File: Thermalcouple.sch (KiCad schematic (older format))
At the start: 14 parts

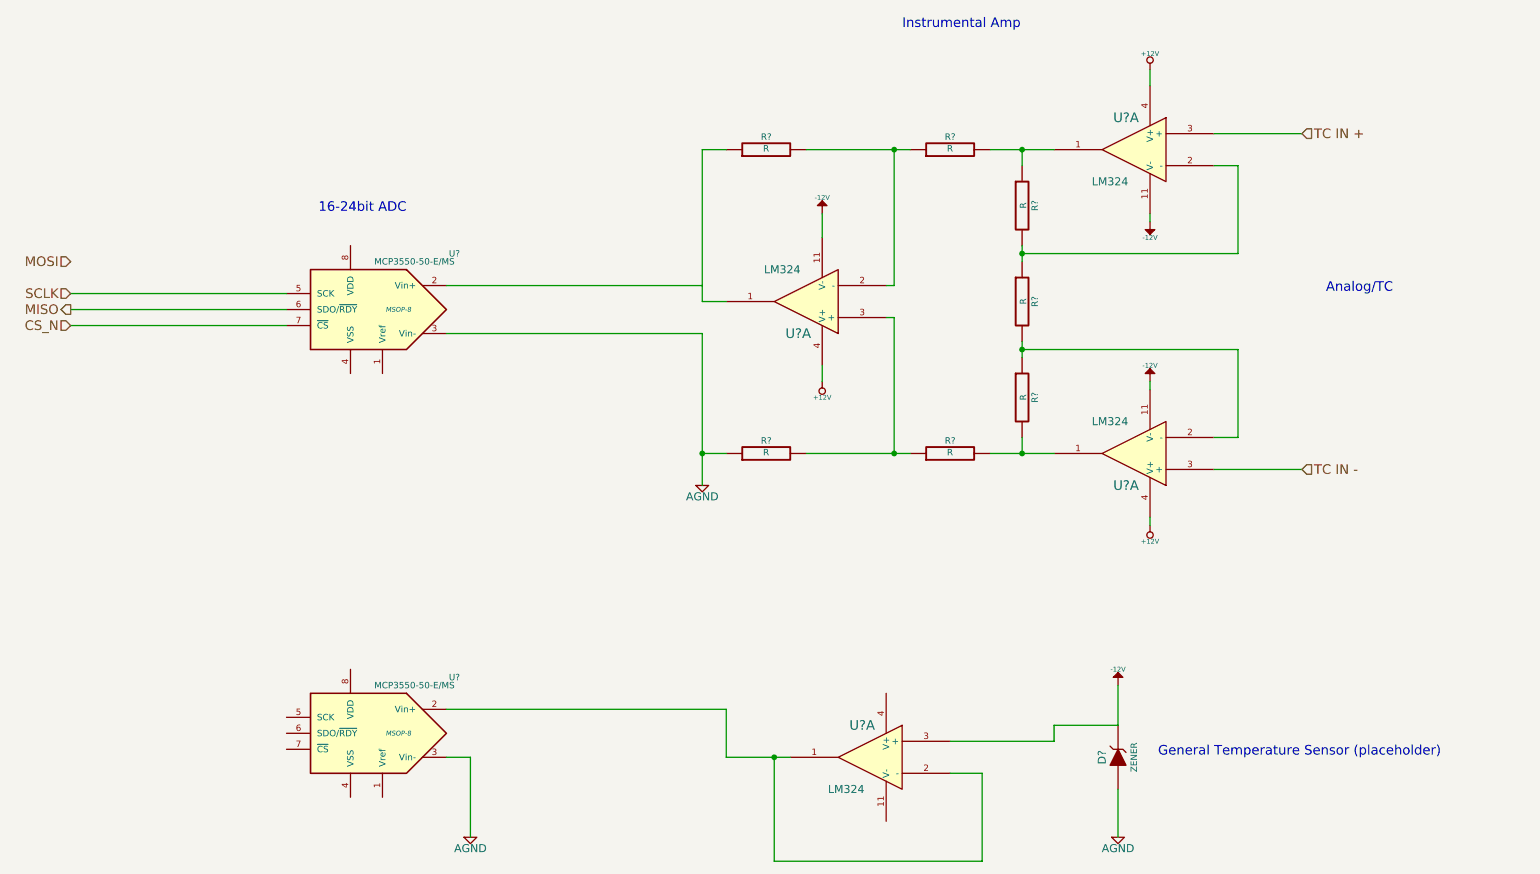
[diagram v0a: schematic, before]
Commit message: associating and placing relay module
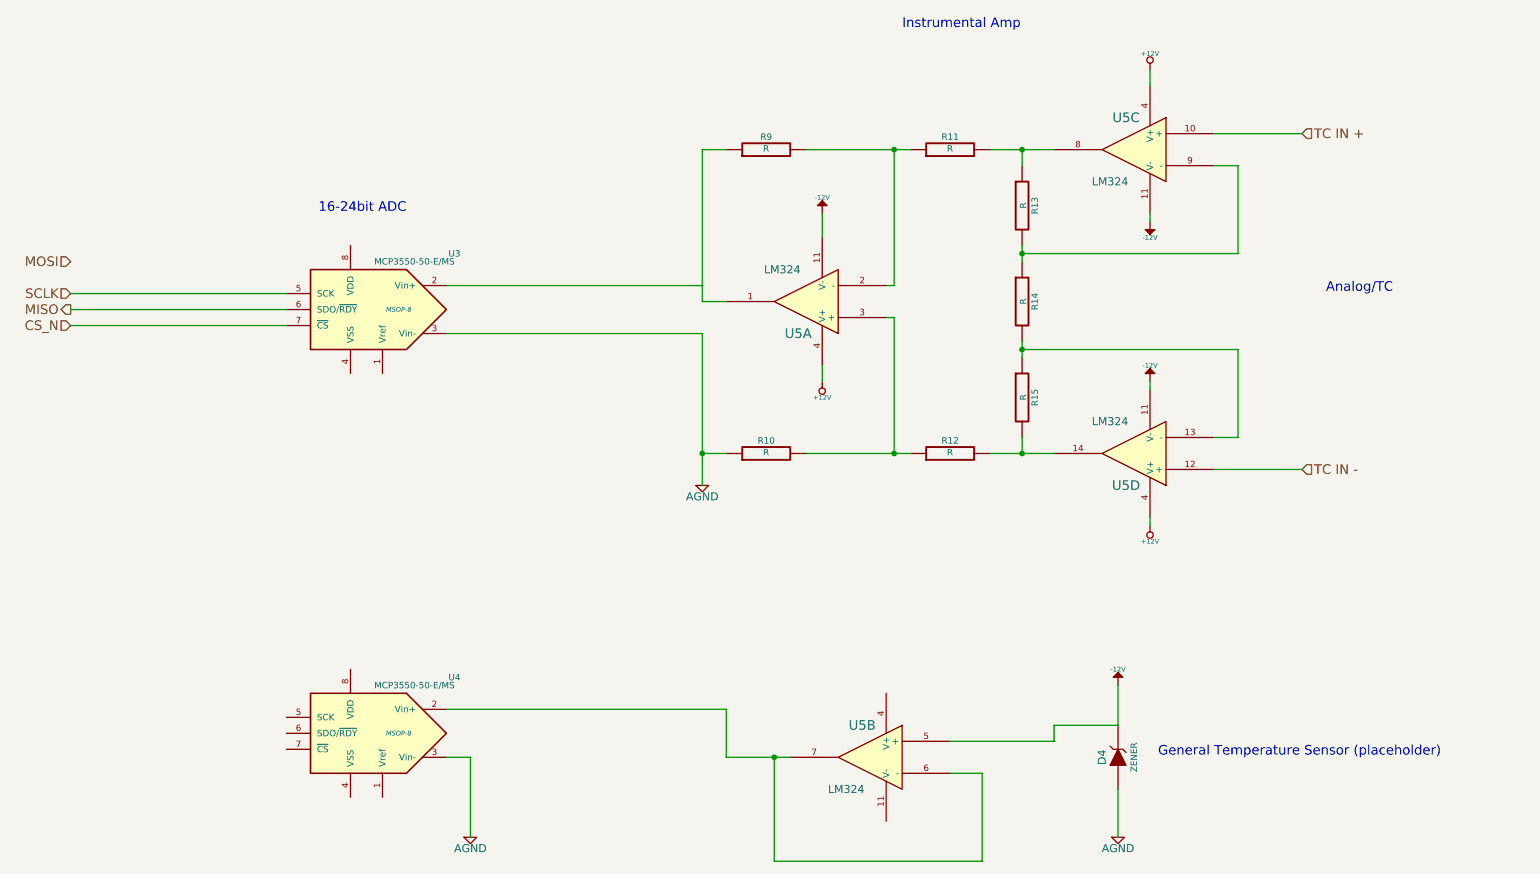
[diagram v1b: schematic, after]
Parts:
- gave numbers to parts that had none: 11
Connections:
- net -12V: now also U5.5 (+); no longer U5.3 (+)
- net TC IN +: now also U5.10 (+); no longer U5.3 (+)
- net TC IN -: now also U5.12 (+); no longer U5.3 (+)
- net at R11.2, R13.1: now also U5.8; no longer U5.1
- net at R13.2, R14.1: now also U5.9 (-); no longer U5.2 (-)
- net at R12.2, R15.2: now also U5.14; no longer U5.1
- net at R14.2, R15.1: now also U5.13 (-); no longer U5.2 (-)
- new net: U4.2 (Vin+), U5.6 (-), U5.7
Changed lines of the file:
@@
 Sheet 8 9
 Title ""
-Date "10 feb 2014"
+Date "22 feb 2014"
 Rev ""
 Comp ""
@@
 CS_N
 $Comp
-L LM324 U?
-U 1 1 52F0F265
+L LM324 U5
+U 3 1 52F0F265
 P 8500 2050
-F 0 "U?" H 8550 2250 60  0000 C CNN
+F 0 "U5" H 8550 2250 60  0000 C CNN
 F 1 "LM324" H 8650 1850 50  0000 C CNN
 F 2 "" H 8500 2050 60  0000 C CNN
 F 3 "" H 8500 2050 60  0000 C CNN
-	1    8500 2050
+	3    8500 2050
 	-1   0    0    -1
 $EndComp
 $Comp
-L LM324 U?
-U 1 1 52F0F27C
+L LM324 U5
+U 4 1 52F0F27C
 P 8500 3950
-F 0 "U?" H 8550 4150 60  0000 C CNN
+F 0 "U5" H 8550 4150 60  0000 C CNN
 F 1 "LM324" H 8650 3750 50  0000 C CNN
 F 2 "" H 8500 3950 60  0000 C CNN
 F 3 "" H 8500 3950 60  0000 C CNN
-	1    8500 3950
-	-1   0    0    1
-$EndComp
-$Comp
-L LM324 U?
+	4    8500 3950
+	-1   0    0    1
+$EndComp
+$Comp
+L LM324 U5
 U 1 1 52F0F282
 P 6450 3000
-F 0 "U?" H 6500 3200 60  0000 C CNN
+F 0 "U5" H 6500 3200 60  0000 C CNN
 F 1 "LM324" H 6600 2800 50  0000 C CNN
 F 2 "" H 6450 3000 60  0000 C CNN
@@
 $EndComp
 $Comp
-L LM324 U?
-U 1 1 52F0F288
+L LM324 U5
+U 2 1 52F0F288
 P 6850 5850
-F 0 "U?" H 6900 6050 60  0000 C CNN
+F 0 "U5" H 6900 6050 60  0000 C CNN
 F 1 "LM324" H 7000 5650 50  0000 C CNN
 F 2 "" H 6850 5850 60  0000 C CNN
 F 3 "" H 6850 5850 60  0000 C CNN
-	1    6850 5850
+	2    6850 5850
 	-1   0    0    -1
 $EndComp
 $Comp
-L R R?
+L R R13
 U 1 1 52F0F311
 P 7800 2400
-F 0 "R?" V 7880 2400 40  0000 C CNN
+F 0 "R13" V 7880 2400 40  0000 C CNN
 F 1 "R" V 7807 2401 40  0000 C CNN
 F 2 "~" V 7730 2400 30  0000 C CNN
@@
 $EndComp
 $Comp
-L R R?
+L R R14
 U 1 1 52F0F317
 P 7800 3000
-F 0 "R?" V 7880 3000 40  0000 C CNN
+F 0 "R14" V 7880 3000 40  0000 C CNN
 F 1 "R" V 7807 3001 40  0000 C CNN
 F 2 "~" V 7730 3000 30  0000 C CNN
@@
 $EndComp
 $Comp
-L R R?
+L R R15
 U 1 1 52F0F31D
 P 7800 3600
-F 0 "R?" V 7880 3600 40  0000 C CNN
+F 0 "R15" V 7880 3600 40  0000 C CNN
 F 1 "R" V 7807 3601 40  0000 C CNN
 F 2 "~" V 7730 3600 30  0000 C CNN
@@
 	7800 3950 7800 3850
 $Comp
-L R R?
+L R R11
 U 1 1 52F0F33D
 P 7350 2050
-F 0 "R?" V 7430 2050 40  0000 C CNN
+F 0 "R11" V 7430 2050 40  0000 C CNN
 F 1 "R" V 7357 2051 40  0000 C CNN
 F 2 "~" V 7280 2050 30  0000 C CNN
@@
 $EndComp
 $Comp
-L R R?
+L R R9
 U 1 1 52F0F349
 P 6200 2050
-F 0 "R?" V 6280 2050 40  0000 C CNN
+F 0 "R9" V 6280 2050 40  0000 C CNN
 F 1 "R" V 6207 2051 40  0000 C CNN
 F 2 "~" V 6130 2050 30  0000 C CNN
@@
 $EndComp
 $Comp
-L R R?
+L R R12
 U 1 1 52F0F360
 P 7350 3950
-F 0 "R?" V 7430 3950 40  0000 C CNN
+F 0 "R12" V 7430 3950 40  0000 C CNN
 F 1 "R" V 7357 3951 40  0000 C CNN
 F 2 "~" V 7280 3950 30  0000 C CNN
@@
 $EndComp
 $Comp
-L R R?
+L R R10
 U 1 1 52F0F366
 P 6200 3950
-F 0 "R?" V 6280 3950 40  0000 C CNN
+F 0 "R10" V 6280 3950 40  0000 C CNN
 F 1 "R" V 6207 3951 40  0000 C CNN
 F 2 "~" V 6130 3950 30  0000 C CNN
@@
 	9550 1950 9000 1950
 $Comp
-L -12V #PWR?
+L -12V #PWR023
 U 1 1 52F0F501
 P 6550 2450
-F 0 "#PWR?" H 6550 2580 20  0001 C CNN
+F 0 "#PWR023" H 6550 2580 20  0001 C CNN
 F 1 "-12V" H 6550 2550 30  0000 C CNN
 F 2 "" H 6550 2450 60  0000 C CNN
@@
 $EndComp
 $Comp
-L -12V #PWR?
+L -12V #PWR024
 U 1 1 52F0F50E
 P 8600 2500
-F 0 "#PWR?" H 8600 2630 20  0001 C CNN
+F 0 "#PWR024" H 8600 2630 20  0001 C CNN
 F 1 "-12V" H 8600 2600 30  0000 C CNN
 F 2 "" H 8600 2500 60  0000 C CNN
@@
 $EndComp
 $Comp
-L -12V #PWR?
+L -12V #PWR025
 U 1 1 52F0F514
 P 8600 3500
-F 0 "#PWR?" H 8600 3630 20  0001 C CNN
+F 0 "#PWR025" H 8600 3630 20  0001 C CNN
 F 1 "-12V" H 8600 3600 30  0000 C CNN
 F 2 "" H 8600 3500 60  0000 C CNN
@@
 	8600 3550 8600 3500
 $Comp
-L +12V #PWR?
+L +12V #PWR026
 U 1 1 52F0F57C
 P 6550 3500
-F 0 "#PWR?" H 6550 3450 20  0001 C CNN
+F 0 "#PWR026" H 6550 3450 20  0001 C CNN
 F 1 "+12V" H 6550 3600 30  0000 C CNN
 F 2 "" H 6550 3500 60  0000 C CNN
@@
 $EndComp
 $Comp
-L +12V #PWR?
+L +12V #PWR027
 U 1 1 52F0F593
 P 8600 4400
-F 0 "#PWR?" H 8600 4350 20  0001 C CNN
+F 0 "#PWR027" H 8600 4350 20  0001 C CNN
 F 1 "+12V" H 8600 4500 30  0000 C CNN
 F 2 "" H 8600 4400 60  0000 C CNN
@@
 $EndComp
 $Comp
-L +12V #PWR?
+L +12V #PWR028
 U 1 1 52F0F599
 P 8600 1550
-F 0 "#PWR?" H 8600 1500 20  0001 C CNN
+F 0 "#PWR028" H 8600 1500 20  0001 C CNN
 F 1 "+12V" H 8600 1650 30  0000 C CNN
 F 2 "" H 8600 1550 60  0000 C CNN
@@
 	6550 3500 6550 3400
 $Comp
-L AGND #PWR?
+L AGND #PWR029
 U 1 1 52F0F60A
 P 5800 4150
-F 0 "#PWR?" H 5800 4150 40  0001 C CNN
+F 0 "#PWR029" H 5800 4150 40  0001 C CNN
 F 1 "AGND" H 5800 4080 50  0000 C CNN
 F 2 "" H 5800 4150 60  0000 C CNN
@@
 	5800 3200 5800 4150
 $Comp
-L MCP3550-50-E/MS U?
+L MCP3550-50-E/MS U3
 U 1 1 52F0F69F
 P 3700 3050
-F 0 "U?" H 3150 3400 40  0000 C CNN
+F 0 "U3" H 3150 3400 40  0000 C CNN
 F 1 "MCP3550-50-E/MS" H 3400 3350 40  0000 C CNN
 F 2 "MSOP-8" H 3500 3050 30  0000 C CIN
@@
 	1850 3150 3200 3150
 $Comp
-L MCP3550-50-E/MS U?
+L MCP3550-50-E/MS U4
 U 1 1 52F0F786
 P 3700 5700
-F 0 "U?" H 3150 6050 40  0000 C CNN
+F 0 "U4" H 3150 6050 40  0000 C CNN
 F 1 "MCP3550-50-E/MS" H 3400 6000 40  0000 C CNN
 F 2 "MSOP-8" H 3500 5700 30  0000 C CIN
@@
 $EndComp
 $Comp
-L ZENER D?
+L ZENER D4
 U 1 1 52F0F78E
 P 8400 5850
-F 0 "D?" H 8400 5950 50  0000 C CNN
+F 0 "D4" H 8400 5950 50  0000 C CNN
 F 1 "ZENER" H 8400 5750 40  0000 C CNN
 F 2 "~" H 8400 5850 60  0000 C CNN
@@
 $EndComp
 $Comp
-L -12V #PWR?
+L -12V #PWR030
 U 1 1 52F0F79B
 P 8400 5400
-F 0 "#PWR?" H 8400 5530 20  0001 C CNN
+F 0 "#PWR030" H 8400 5530 20  0001 C CNN
 F 1 "-12V" H 8400 5500 30  0000 C CNN
 F 2 "" H 8400 5400 60  0000 C CNN
@@
 $EndComp
 $Comp
-L AGND #PWR?
+L AGND #PWR031
 U 1 1 52F0F7A1
 P 8400 6350
-F 0 "#PWR?" H 8400 6350 40  0001 C CNN
+F 0 "#PWR031" H 8400 6350 40  0001 C CNN
 F 1 "AGND" H 8400 6280 50  0000 C CNN
 F 2 "" H 8400 6350 60  0000 C CNN
@@
 Connection ~ 6250 5850
 $Comp
-L AGND #PWR?
+L AGND #PWR032
 U 1 1 52F0F89A
 P 4350 6350
-F 0 "#PWR?" H 4350 6350 40  0001 C CNN
+F 0 "#PWR032" H 4350 6350 40  0001 C CNN
 F 1 "AGND" H 4350 6280 50  0000 C CNN
 F 2 "" H 4350 6350 60  0000 C CNN
